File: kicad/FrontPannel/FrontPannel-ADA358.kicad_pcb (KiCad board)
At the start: 2 copper layers, 198 x 58 mm, 18 parts

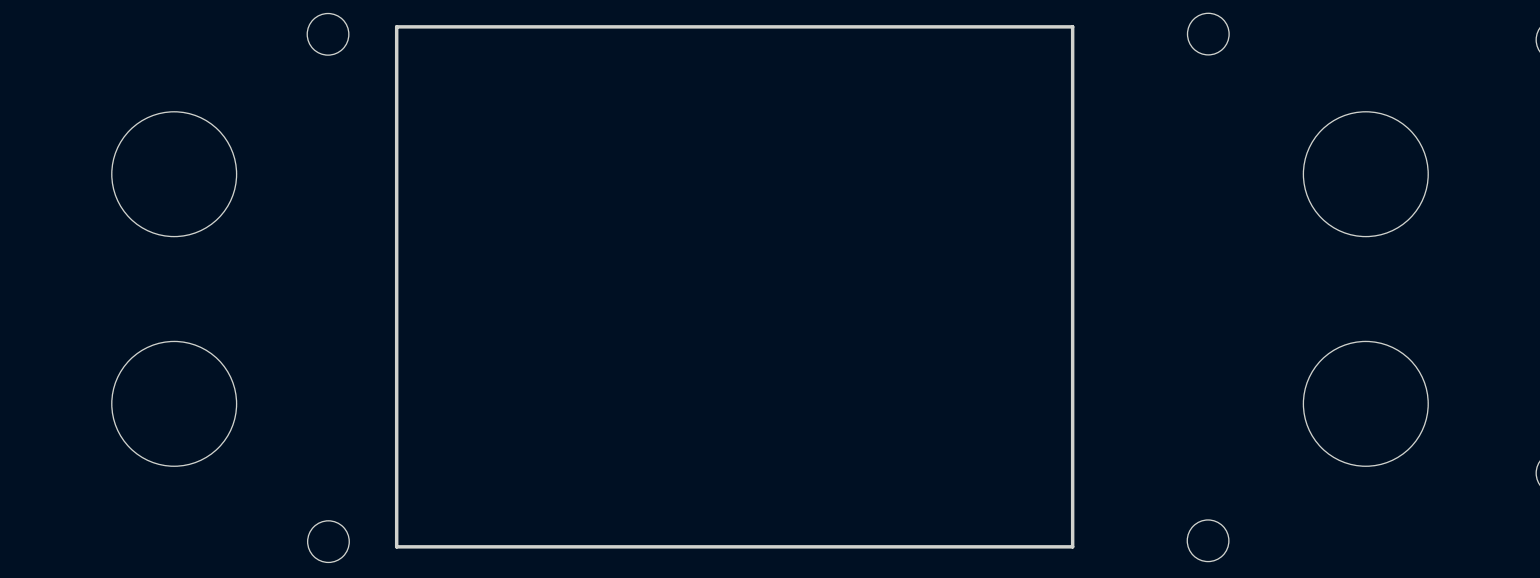
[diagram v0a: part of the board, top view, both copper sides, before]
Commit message: New front panel (#86)
v0.2 of front panel. light up led buttons, new adc, new i/o expander
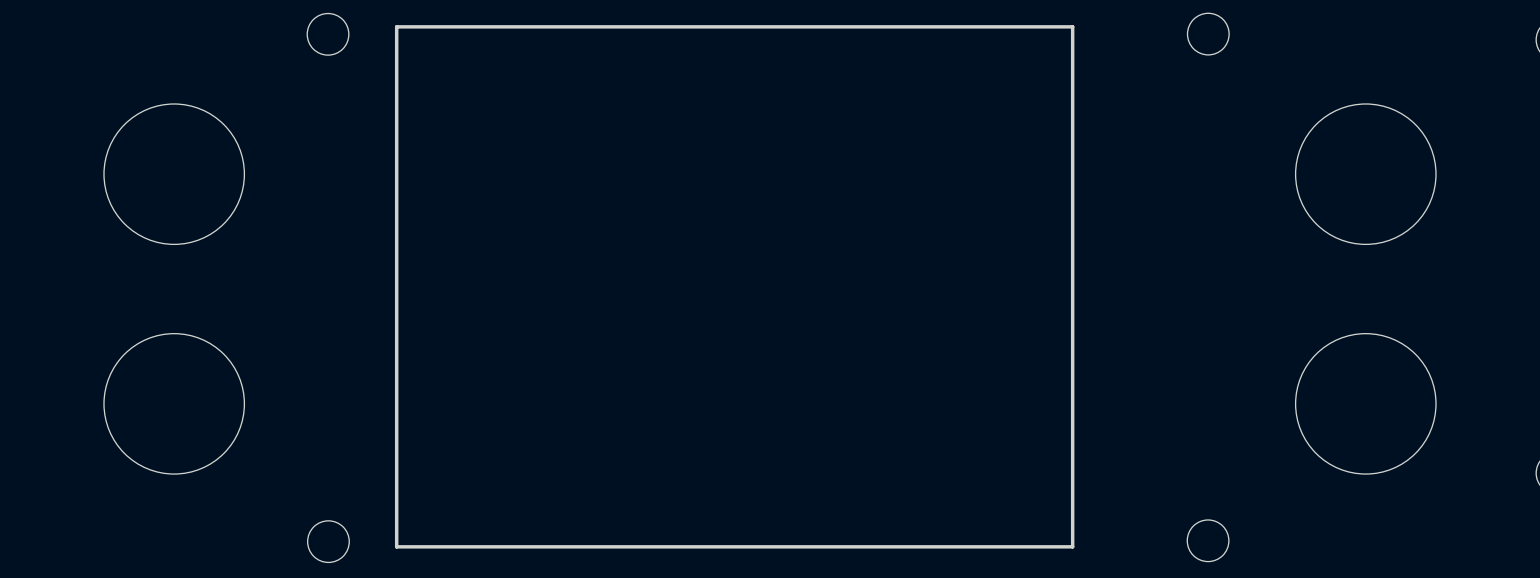
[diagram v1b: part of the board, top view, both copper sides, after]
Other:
- board text added: "ZC95 Front panel v0.3"
- board text removed: "ZC95 Front panel v0.2"
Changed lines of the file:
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@@
       (drillshape 0)
       (scaleselection 1)
-      (outputdirectory "gerber/FP/")
+      (outputdirectory "FAB/")
     )
   )
@@
     (fp_circle (center 0 0) (end 2.2 0) (layer "Cmts.User") (width 0.15) (fill none))
     (fp_circle (center 0 0) (end 2.45 0) (layer "F.CrtYd") (width 0.05) (fill none))
-    (pad "" np_thru_hole circle locked (at 0 0) (size 7.2 7.2) (drill 7.2) (layers *.Cu *.Mask))
+    (pad "" np_thru_hole circle locked (at 0 0) (size 8.1 8.1) (drill 8.1) (layers F&B.Cu *.Mask))
   )
   (footprint "MountingHole:MountingHole_2.2mm_M2" (layer "F.Cu")
@@
     (fp_circle (center 0 0) (end 2.2 0) (layer "Cmts.User") (width 0.15) (fill none))
     (fp_circle (center 0 0) (end 2.45 0) (layer "F.CrtYd") (width 0.05) (fill none))
-    (pad "" np_thru_hole circle locked (at 0 0) (size 7.2 7.2) (drill 7.2) (layers *.Cu *.Mask))
+    (pad "" np_thru_hole circle locked (at 0 0) (size 8.1 8.1) (drill 8.1) (layers F&B.Cu *.Mask))
   )
   (footprint "MountingHole:MountingHole_2.2mm_M2" (layer "F.Cu")
@@
     (fp_line (start -3.05 -9.1) (end 12.15 -9.1) (layer "Edge.Cuts") (width 0.12))
     (fp_line (start 13.78204 -7.13232) (end 12.95 -0.45) (layer "Edge.Cuts") (width 0.12))
-    (fp_arc (start -2.2 0.95) (mid -3.267027 0.561634) (end -3.834781 -0.421744) (layer "Edge.Cuts") (width 0.12))
+    (fp_arc (start -2.2 0.95) (mid -3.267028 0.561634) (end -3.834781 -0.421744) (layer "Edge.Cuts") (width 0.12))
     (fp_arc (start -4.684781 -7.151744) (mid -4.321634 -8.507028) (end -3.05 -9.1) (layer "Edge.Cuts") (width 0.12))
     (fp_arc (start 12.934781 -0.421744) (mid 12.367028 0.561634) (end 11.3 0.95) (layer "Edge.Cuts") (width 0.12))
@@
     (fp_circle (center 0 0) (end 2.2 0) (layer "Cmts.User") (width 0.15) (fill none))
     (fp_circle (center 0 0) (end 2.45 0) (layer "F.CrtYd") (width 0.05) (fill none))
-    (pad "" np_thru_hole circle locked (at 0 0) (size 7.2 7.2) (drill 7.2) (layers *.Cu *.Mask))
+    (pad "" np_thru_hole circle locked (at 0 0) (size 8.1 8.1) (drill 8.1) (layers F&B.Cu *.Mask))
   )
   (footprint "MountingHole:MountingHole_2.2mm_M2" (layer "F.Cu")
@@
     (fp_circle (center 0 0) (end 2.2 0) (layer "Cmts.User") (width 0.15) (fill none))
     (fp_circle (center 0 0) (end 2.45 0) (layer "F.CrtYd") (width 0.05) (fill none))
-    (pad "" np_thru_hole circle locked (at 0 0) (size 7.2 7.2) (drill 7.2) (layers *.Cu *.Mask))
+    (pad "" np_thru_hole circle locked (at 0 0) (size 8.1 8.1) (drill 8.1) (layers F&B.Cu *.Mask))
   )
   (footprint "MountingHole:MountingHole_2.2mm_M2" (layer "F.Cu")
@@
     (effects (font (size 1.5 1.5) (thickness 0.3)))
   )
-  (gr_text "ZC95 \nFront panel\nv0.2" (at 157 116.5) (layer "B.SilkS")
+  (gr_text "ZC95 \nFront panel\nv0.3" (at 157 116.5) (layer "B.SilkS")
     (effects (font (size 1.5 1.5) (thickness 0.3)) (justify mirror))
   )
